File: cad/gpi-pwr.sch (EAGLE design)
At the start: 104 parts, among them CN1 HEADER-1X2, CN2 HEADER-3X1, CN3 HEADER-1X2.4, CN4 HEADER-3X12MM, Q1 MOSFETTO247REV, Q3 MOSFETTO247REV, Q5 MOSFETTO247REV, Q6 MOSFETTO247REV, Q7 MOSFETTO247REV, Q8 MOSFETTO247REV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

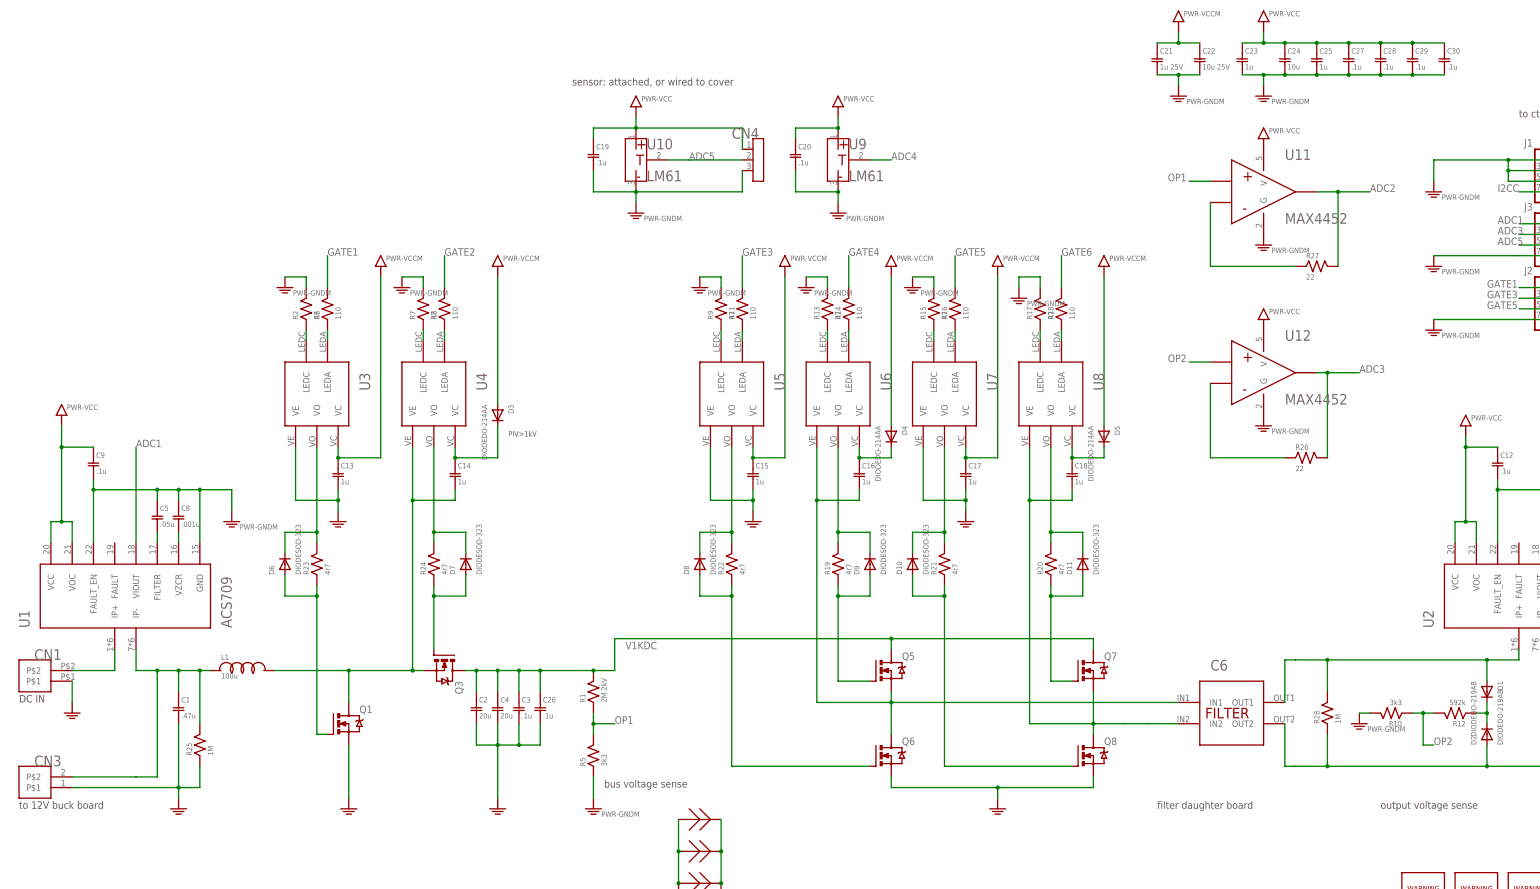
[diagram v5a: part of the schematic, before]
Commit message: revert opamp, tweak
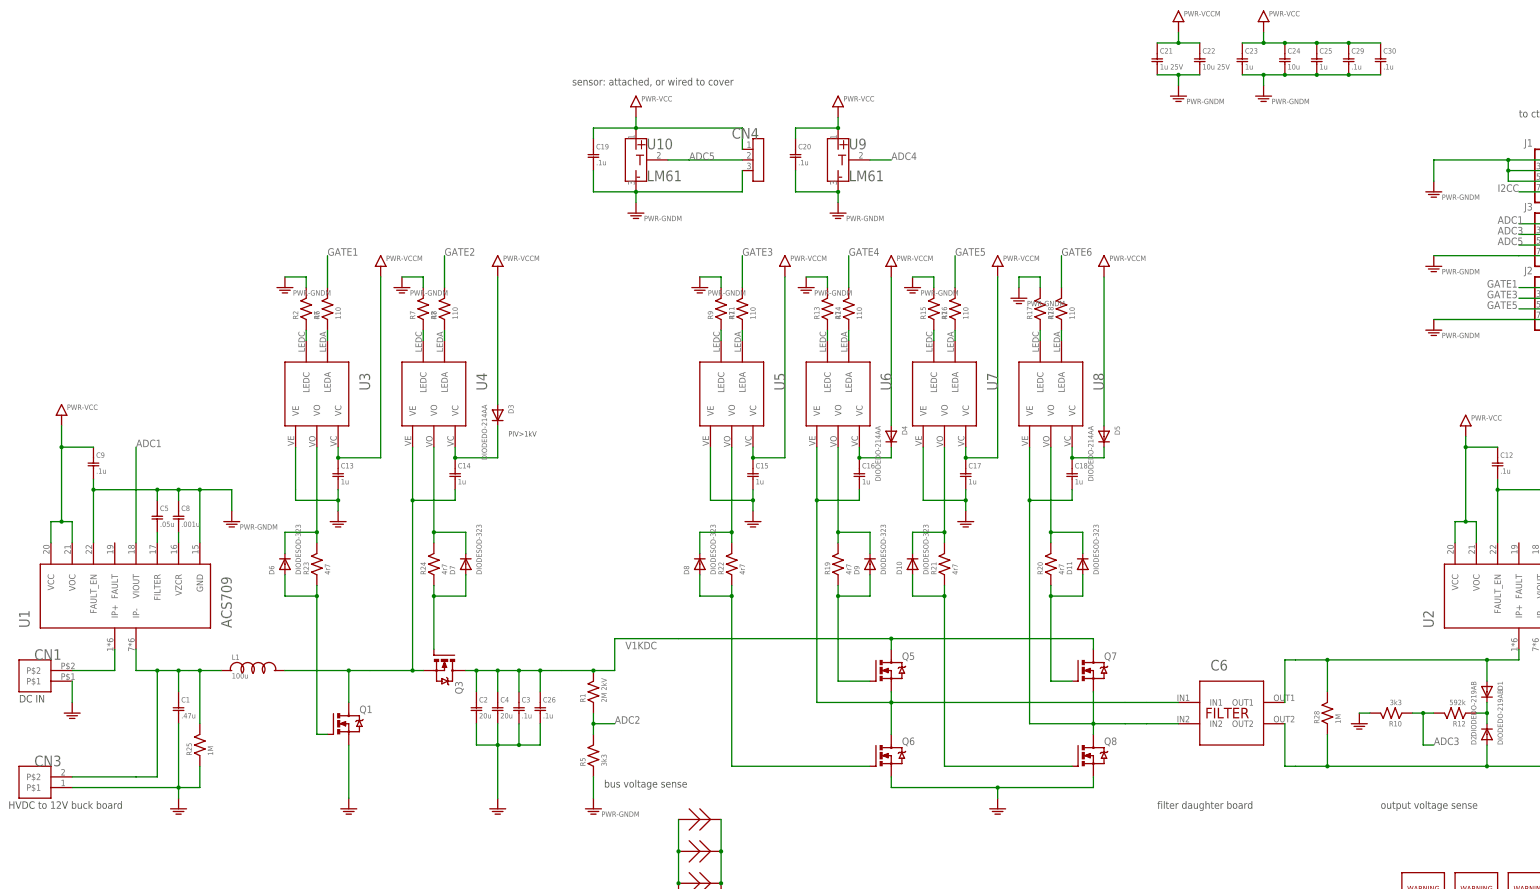
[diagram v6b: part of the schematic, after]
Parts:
- removed C27, C28: .1u, jaw:C0603
- removed R26, R27: 22, jaw:R0603
- removed U11, U12: MAX4452, jaw:OPAMP
- Q1, Q3, Q5, Q6, Q7, Q8: value MOSFETTO247REV -> C2M0160120D
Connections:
- removed net N$51: R26.P$1, U12.INM
- removed net N$52: R27.P$1, U11.INM
- removed net OP1: R1.P$1, R5.P$2, U11.INP
- removed net OP2: R10.P$1, R12.P$2, U12.INP
- net ADC2: now also R1.P$1, R5.P$2; no longer R27.P$2, U11.OUT
- net ADC3: now also R10.P$1, R12.P$2; no longer R26.P$2, U12.OUT
- net GND: now also R10.P$2
- net GNDM: no longer C27.P$2, C28.P$2, R10.P$2, U11.G, U12.G
- net VCC: no longer C27.P$1, C28.P$1, U11.V, U12.V
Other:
- note added: "HVDC to 12V buck board"
- note removed: "to 12V buck board"
- moved on the sheet: C29, C30, L1

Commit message: readme, clean
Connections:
- net GND: now also R5.P$1
- net GNDM: no longer R5.P$1
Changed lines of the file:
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@@
 <layer number="54" name="bGND_GNDA" color="7" fill="1" visible="no" active="no"/>
 <layer number="56" name="wert" color="7" fill="1" visible="no" active="no"/>
+<layer number="57" name="tCAD" color="7" fill="1" visible="no" active="no"/>
+<layer number="59" name="tCarbon" color="7" fill="1" visible="no" active="no"/>
+<layer number="60" name="bCarbon" color="7" fill="1" visible="no" active="no"/>
 <layer number="90" name="Modules" color="5" fill="1" visible="yes" active="yes"/>
 <layer number="91" name="Nets" color="2" fill="1" visible="yes" active="yes"/>
@@
 <layer number="97" name="Info" color="7" fill="1" visible="yes" active="yes"/>
 <layer number="98" name="Guide" color="6" fill="1" visible="yes" active="yes"/>
+<layer number="99" name="SpiceOrder" color="7" fill="1" visible="no" active="no"/>
 <layer number="100" name="Muster" color="7" fill="1" visible="yes" active="yes"/>
 <layer number="101" name="Hidden" color="15" fill="1" visible="yes" active="yes"/>
@@
 <layer number="111" name="LPC17xx" color="7" fill="1" visible="yes" active="yes"/>
 <layer number="112" name="tSilk" color="7" fill="1" visible="yes" active="yes"/>
+<layer number="113" name="ReferenceLS" color="7" fill="1" visible="no" active="no"/>
 <layer number="116" name="Patch_BOT" color="7" fill="1" visible="yes" active="yes"/>
+<layer number="118" name="Rect_Pads" color="7" fill="1" visible="no" active="no"/>
 <layer number="121" name="_tsilk" color="7" fill="1" visible="yes" active="yes"/>
 <layer number="122" name="_bsilk" color="7" fill="1" visible="yes" active="yes"/>
@@
 <layer number="127" name="_tValues" color="7" fill="1" visible="yes" active="yes"/>
 <layer number="128" name="_bValues" color="7" fill="1" visible="yes" active="yes"/>
+<layer number="129" name="Mask" color="7" fill="1" visible="yes" active="yes"/>
 <layer number="131" name="prix" color="7" fill="1" visible="yes" active="yes"/>
 <layer number="132" name="test" color="7" fill="1" visible="yes" active="yes"/>
 <layer number="144" name="Drill_legend" color="7" fill="1" visible="yes" active="yes"/>
+<layer number="150" name="Notes" color="7" fill="1" visible="no" active="yes"/>
 <layer number="151" name="HeatSink" color="7" fill="1" visible="yes" active="yes"/>
 <layer number="152" name="_bDocu" color="7" fill="1" visible="yes" active="yes"/>
+<layer number="153" name="FabDoc1" color="6" fill="1" visible="no" active="no"/>
+<layer number="154" name="FabDoc2" color="2" fill="1" visible="no" active="no"/>
+<layer number="155" name="FabDoc3" color="7" fill="15" visible="no" active="no"/>
 <layer number="199" name="Contour" color="7" fill="1" visible="yes" active="yes"/>
 <layer number="200" name="200bmp" color="7" fill="1" visible="yes" active="yes"/>
@@
 <layer number="223" name="223bmp" color="24" fill="1" visible="no" active="no"/>
 <layer number="224" name="224bmp" color="25" fill="1" visible="no" active="no"/>
+<layer number="225" name="225bmp" color="7" fill="1" visible="yes" active="yes"/>
+<layer number="226" name="226bmp" color="7" fill="1" visible="yes" active="yes"/>
+<layer number="227" name="227bmp" color="7" fill="1" visible="yes" active="yes"/>
+<layer number="228" name="228bmp" color="7" fill="1" visible="yes" active="yes"/>
+<layer number="229" name="229bmp" color="7" fill="1" visible="yes" active="yes"/>
+<layer number="230" name="230bmp" color="7" fill="1" visible="yes" active="yes"/>
+<layer number="231" name="Eagle3D_PG1" color="7" fill="1" visible="no" active="no"/>
+<layer number="232" name="Eagle3D_PG2" color="7" fill="1" visible="no" active="no"/>
+<layer number="233" name="Eagle3D_PG3" color="7" fill="1" visible="no" active="no"/>
 <layer number="248" name="Housing" color="7" fill="1" visible="yes" active="yes"/>
 <layer number="249" name="Edge" color="7" fill="1" visible="yes" active="yes"/>
@@
 <layer number="251" name="SMDround" color="7" fill="1" visible="yes" active="yes"/>
 <layer number="254" name="cooling" color="7" fill="1" visible="yes" active="yes"/>
+<layer number="255" name="routoute" color="7" fill="1" visible="yes" active="yes"/>
 </layers>
 <schematic xreflabel="%F%N/%S.%C%R" xrefpart="/%S.%C%R">
@@
 <part name="GNDM12" library="jaw" deviceset="PWR-GNDM" device=""/>
 <part name="GNDM1" library="jaw" deviceset="PWR-GNDM" device=""/>
-<part name="GNDM13" library="jaw" deviceset="PWR-GNDM" device=""/>
 <part name="GNDM14" library="jaw" deviceset="PWR-GNDM" device=""/>
 <part name="GNDM15" library="jaw" deviceset="PWR-GNDM" device=""/>
@@
 <part name="C6" library="jaw-brd" deviceset="FILTER" device=""/>
 <part name="GND10" library="jaw" deviceset="PWR-GND" device=""/>
+<part name="GND11" library="jaw" deviceset="PWR-GND" device=""/>
 </parts>
 <sheets>
@@
 <instance part="GNDM12" gate="G$1" x="246.38" y="185.42"/>
 <instance part="GNDM1" gate="G$1" x="58.42" y="132.08"/>
-<instance part="GNDM13" gate="G$1" x="144.78" y="63.5"/>
 <instance part="GNDM14" gate="G$1" x="154.94" y="205.74"/>
 <instance part="GNDM15" gate="G$1" x="203.2" y="205.74"/>
@@
 <instance part="C6" gate="G$1" x="297.18" y="86.36"/>
 <instance part="GND10" gate="G$1" x="327.66" y="83.82"/>
+<instance part="GND11" gate="G$1" x="144.78" y="63.5"/>
 </instances>
 <busses>
@@
 <wire x1="330.2" y1="86.36" x2="327.66" y2="86.36" width="0.1524" layer="91"/>
 <pinref part="GND10" gate="G$1" pin="GND"/>
+</segment>
+<segment>
+<pinref part="R5" gate="G$1" pin="P$1"/>
+<wire x1="144.78" y1="66.04" x2="144.78" y2="71.12" width="0.1524" layer="91"/>
+<pinref part="GND11" gate="G$1" pin="GND"/>
 </segment>
 </net>
@@
 </segment>
 <segment>
-<pinref part="R5" gate="G$1" pin="P$1"/>
-<wire x1="144.78" y1="66.04" x2="144.78" y2="71.12" width="0.1524" layer="91"/>
-<pinref part="GNDM13" gate="G$1" pin="GNDM"/>
-</segment>
-<segment>
